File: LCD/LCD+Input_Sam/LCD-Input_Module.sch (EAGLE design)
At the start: 23 parts

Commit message: LCD PCB final touches
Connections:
- removed net N$1: JP2.3
- removed net N$2: JP2.2
- removed net N$3: JP2.1
- removed net N$8: JP2.4
- net !RES: now also JP2.3
- net SA0: now also JP2.4
- net SCL: now also JP2.2
- net SDA: now also JP2.1
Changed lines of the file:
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@@
 <grid distance="0.1" unitdist="inch" unit="inch" style="lines" multiple="1" display="no" altdistance="0.01" altunitdist="inch" altunit="inch"/>
 <layers>
-<layer number="1" name="Top" color="4" fill="1" visible="no" active="no"/>
-<layer number="16" name="Bottom" color="1" fill="1" visible="no" active="no"/>
-<layer number="17" name="Pads" color="2" fill="1" visible="no" active="no"/>
-<layer number="18" name="Vias" color="2" fill="1" visible="no" active="no"/>
-<layer number="19" name="Unrouted" color="6" fill="1" visible="no" active="no"/>
-<layer number="20" name="Dimension" color="24" fill="1" visible="no" active="no"/>
-<layer number="21" name="tPlace" color="7" fill="1" visible="no" active="no"/>
-<layer number="22" name="bPlace" color="7" fill="1" visible="no" active="no"/>
-<layer number="23" name="tOrigins" color="15" fill="1" visible="no" active="no"/>
-<layer number="24" name="bOrigins" color="15" fill="1" visible="no" active="no"/>
-<layer number="25" name="tNames" color="7" fill="1" visible="no" active="no"/>
-<layer number="26" name="bNames" color="7" fill="1" visible="no" active="no"/>
-<layer number="27" name="tValues" color="7" fill="1" visible="no" active="no"/>
-<layer number="28" name="bValues" color="7" fill="1" visible="no" active="no"/>
+<layer number="1" name="Top" color="4" fill="1" visible="yes" active="no"/>
+<layer number="16" name="Bottom" color="1" fill="1" visible="yes" active="no"/>
+<layer number="17" name="Pads" color="2" fill="1" visible="yes" active="no"/>
+<layer number="18" name="Vias" color="2" fill="1" visible="yes" active="no"/>
+<layer number="19" name="Unrouted" color="6" fill="1" visible="yes" active="no"/>
+<layer number="20" name="Dimension" color="24" fill="1" visible="yes" active="no"/>
+<layer number="21" name="tPlace" color="7" fill="1" visible="yes" active="no"/>
+<layer number="22" name="bPlace" color="7" fill="1" visible="yes" active="no"/>
+<layer number="23" name="tOrigins" color="15" fill="1" visible="yes" active="no"/>
+<layer number="24" name="bOrigins" color="15" fill="1" visible="yes" active="no"/>
+<layer number="25" name="tNames" color="7" fill="1" visible="yes" active="no"/>
+<layer number="26" name="bNames" color="7" fill="1" visible="yes" active="no"/>
+<layer number="27" name="tValues" color="7" fill="1" visible="yes" active="no"/>
+<layer number="28" name="bValues" color="7" fill="1" visible="yes" active="no"/>
 <layer number="29" name="tStop" color="7" fill="3" visible="no" active="no"/>
 <layer number="30" name="bStop" color="7" fill="6" visible="no" active="no"/>
@@
 <layer number="35" name="tGlue" color="7" fill="4" visible="no" active="no"/>
 <layer number="36" name="bGlue" color="7" fill="5" visible="no" active="no"/>
-<layer number="37" name="tTest" color="7" fill="1" visible="no" active="no"/>
-<layer number="38" name="bTest" color="7" fill="1" visible="no" active="no"/>
+<layer number="37" name="tTest" color="7" fill="1" visible="yes" active="no"/>
+<layer number="38" name="bTest" color="7" fill="1" visible="yes" active="no"/>
 <layer number="39" name="tKeepout" color="4" fill="11" visible="no" active="no"/>
 <layer number="40" name="bKeepout" color="1" fill="11" visible="no" active="no"/>
@@
 <layer number="44" name="Drills" color="7" fill="1" visible="no" active="no"/>
 <layer number="45" name="Holes" color="7" fill="1" visible="no" active="no"/>
-<layer number="46" name="Milling" color="3" fill="1" visible="no" active="no"/>
-<layer number="47" name="Measures" color="7" fill="1" visible="no" active="no"/>
-<layer number="48" name="Document" color="7" fill="1" visible="no" active="no"/>
-<layer number="49" name="Reference" color="7" fill="1" visible="no" active="no"/>
-<layer number="51" name="tDocu" color="7" fill="1" visible="no" active="no"/>
-<layer number="52" name="bDocu" color="7" fill="1" visible="no" active="no"/>
+<layer number="46" name="Milling" color="3" fill="1" visible="yes" active="no"/>
+<layer number="47" name="Measures" color="7" fill="1" visible="yes" active="no"/>
+<layer number="48" name="Document" color="7" fill="1" visible="yes" active="no"/>
+<layer number="49" name="Reference" color="7" fill="1" visible="yes" active="no"/>
+<layer number="51" name="tDocu" color="7" fill="1" visible="yes" active="no"/>
+<layer number="52" name="bDocu" color="7" fill="1" visible="yes" active="no"/>
 <layer number="88" name="SimResults" color="9" fill="1" visible="yes" active="yes"/>
 <layer number="89" name="SimProbes" color="9" fill="1" visible="yes" active="yes"/>
@@
 <net name="SDA" class="0">
 <segment>
-<wire x1="65" y1="32.36" x2="65" y2="32.395" width="0.1524" layer="91"/>
-<label x="65.2" y="32.37" size="1.778" layer="95" rot="R180"/>
-</segment>
-<segment>
 <pinref part="U$1" gate="G$1" pin="D2"/>
 <wire x1="47.2" y1="47.565" x2="47.2" y2="46" width="0.1524" layer="91"/>
@@
 <wire x1="49" y1="46" x2="49" y2="30.48" width="0.1524" layer="91"/>
 <wire x1="49" y1="30.48" x2="48.26" y2="30.48" width="0.1524" layer="91"/>
+</segment>
+<segment>
+<pinref part="JP2" gate="A" pin="1"/>
+<wire x1="88.9" y1="33.02" x2="81.28" y2="33.02" width="0.1524" layer="91"/>
+<label x="76.2" y="33.02" size="1.778" layer="95"/>
 </segment>
 </net>
@@
 <net name="!RES" class="0">
 <segment>
-<wire x1="65.375" y1="27.28" x2="65.375" y2="27.22" width="0.1524" layer="91"/>
-<label x="65.4" y="26.82" size="1.778" layer="95" rot="R180"/>
-</segment>
-<segment>
 <pinref part="U$1" gate="G$1" pin="!RESET"/>
 <wire x1="69.66" y1="57.025" x2="69.66" y2="57" width="0.1524" layer="91"/>
@@
 <label x="73" y="57" size="1.778" layer="95"/>
 </segment>
+<segment>
+<pinref part="JP2" gate="A" pin="3"/>
+<wire x1="81.28" y1="27.94" x2="88.9" y2="27.94" width="0.1524" layer="91"/>
+<label x="73.66" y="27.94" size="1.778" layer="95"/>
+</segment>
 </net>
 <net name="SCL" class="0">
-<segment>
-<wire x1="64.875" y1="29.82" x2="64.875" y2="30.02" width="0.1524" layer="91"/>
-<label x="65.4" y="29.82" size="1.778" layer="95" rot="R180"/>
-</segment>
 <segment>
 <pinref part="R8" gate="G$1" pin="2"/>
@@
 <wire x1="51.2" y1="25.4" x2="51.2" y2="47.565" width="0.1524" layer="91"/>
 <label x="51" y="25" size="1.778" layer="95" rot="R180"/>
+</segment>
+<segment>
+<pinref part="JP2" gate="A" pin="2"/>
+<wire x1="81.28" y1="30.48" x2="88.9" y2="30.48" width="0.1524" layer="91"/>
+<label x="76.2" y="30.48" size="1.778" layer="95"/>
 </segment>
 </net>
@@
 <label x="60.96" y="45.72" size="1.778" layer="95"/>
 </segment>
-</net>
-<net name="N$1" class="0">
-<segment>
-<pinref part="JP2" gate="A" pin="3"/>
-<wire x1="66.04" y1="27.94" x2="88.9" y2="27.94" width="0.1524" layer="91"/>
-</segment>
-</net>
-<net name="N$2" class="0">
-<segment>
-<pinref part="JP2" gate="A" pin="2"/>
-<wire x1="66.04" y1="30.48" x2="88.9" y2="30.48" width="0.1524" layer="91"/>
-</segment>
-</net>
-<net name="N$3" class="0">
-<segment>
-<pinref part="JP2" gate="A" pin="1"/>
-<wire x1="66.04" y1="33.02" x2="88.9" y2="33.02" width="0.1524" layer="91"/>
-</segment>
-</net>
-<net name="N$8" class="0">
 <segment>
 <pinref part="JP2" gate="A" pin="4"/>
-<wire x1="88.9" y1="25.4" x2="66.04" y2="25.4" width="0.1524" layer="91"/>
-</segment>
-</net>
+<wire x1="88.9" y1="25.4" x2="81.28" y2="25.4" width="0.1524" layer="91"/>
+<label x="76.2" y="25.4" size="1.778" layer="95"/>
+</segment>
+</net>

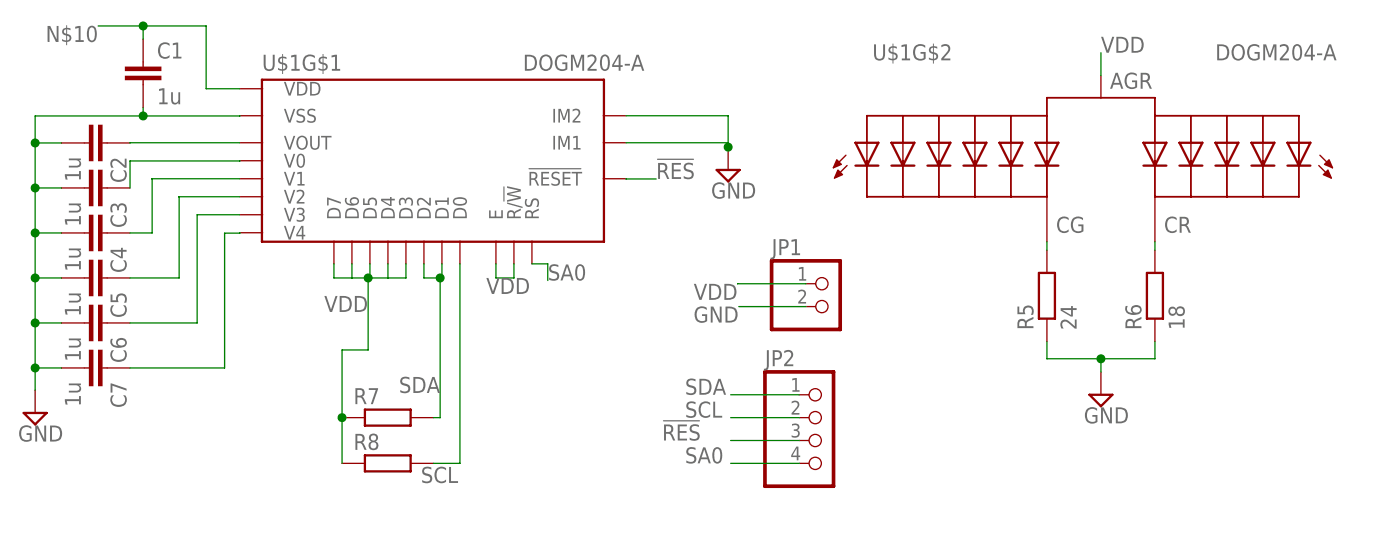
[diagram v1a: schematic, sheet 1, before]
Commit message: LCD PCB changes according to Robins suggestions. Still pending one thing
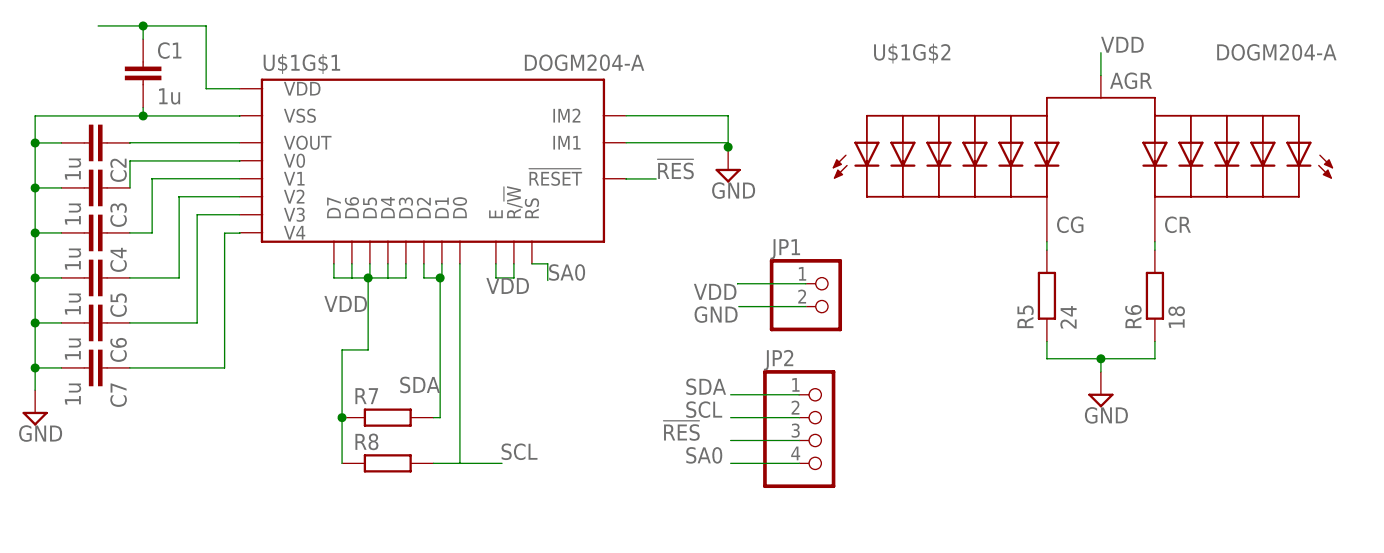
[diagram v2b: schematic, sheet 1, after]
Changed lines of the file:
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@@
 <grid distance="0.1" unitdist="inch" unit="inch" style="lines" multiple="1" display="no" altdistance="0.01" altunitdist="inch" altunit="inch"/>
 <layers>
-<layer number="1" name="Top" color="4" fill="1" visible="yes" active="no"/>
-<layer number="16" name="Bottom" color="1" fill="1" visible="yes" active="no"/>
-<layer number="17" name="Pads" color="2" fill="1" visible="yes" active="no"/>
-<layer number="18" name="Vias" color="2" fill="1" visible="yes" active="no"/>
-<layer number="19" name="Unrouted" color="6" fill="1" visible="yes" active="no"/>
-<layer number="20" name="Dimension" color="24" fill="1" visible="yes" active="no"/>
-<layer number="21" name="tPlace" color="7" fill="1" visible="yes" active="no"/>
-<layer number="22" name="bPlace" color="7" fill="1" visible="yes" active="no"/>
-<layer number="23" name="tOrigins" color="15" fill="1" visible="yes" active="no"/>
-<layer number="24" name="bOrigins" color="15" fill="1" visible="yes" active="no"/>
-<layer number="25" name="tNames" color="7" fill="1" visible="yes" active="no"/>
-<layer number="26" name="bNames" color="7" fill="1" visible="yes" active="no"/>
-<layer number="27" name="tValues" color="7" fill="1" visible="yes" active="no"/>
-<layer number="28" name="bValues" color="7" fill="1" visible="yes" active="no"/>
+<layer number="1" name="Top" color="4" fill="1" visible="no" active="no"/>
+<layer number="16" name="Bottom" color="1" fill="1" visible="no" active="no"/>
+<layer number="17" name="Pads" color="2" fill="1" visible="no" active="no"/>
+<layer number="18" name="Vias" color="2" fill="1" visible="no" active="no"/>
+<layer number="19" name="Unrouted" color="6" fill="1" visible="no" active="no"/>
+<layer number="20" name="Dimension" color="24" fill="1" visible="no" active="no"/>
+<layer number="21" name="tPlace" color="7" fill="1" visible="no" active="no"/>
+<layer number="22" name="bPlace" color="7" fill="1" visible="no" active="no"/>
+<layer number="23" name="tOrigins" color="15" fill="1" visible="no" active="no"/>
+<layer number="24" name="bOrigins" color="15" fill="1" visible="no" active="no"/>
+<layer number="25" name="tNames" color="7" fill="1" visible="no" active="no"/>
+<layer number="26" name="bNames" color="7" fill="1" visible="no" active="no"/>
+<layer number="27" name="tValues" color="7" fill="1" visible="no" active="no"/>
+<layer number="28" name="bValues" color="7" fill="1" visible="no" active="no"/>
 <layer number="29" name="tStop" color="7" fill="3" visible="no" active="no"/>
 <layer number="30" name="bStop" color="7" fill="6" visible="no" active="no"/>
@@
 <layer number="35" name="tGlue" color="7" fill="4" visible="no" active="no"/>
 <layer number="36" name="bGlue" color="7" fill="5" visible="no" active="no"/>
-<layer number="37" name="tTest" color="7" fill="1" visible="yes" active="no"/>
-<layer number="38" name="bTest" color="7" fill="1" visible="yes" active="no"/>
+<layer number="37" name="tTest" color="7" fill="1" visible="no" active="no"/>
+<layer number="38" name="bTest" color="7" fill="1" visible="no" active="no"/>
 <layer number="39" name="tKeepout" color="4" fill="11" visible="no" active="no"/>
 <layer number="40" name="bKeepout" color="1" fill="11" visible="no" active="no"/>
@@
 <layer number="44" name="Drills" color="7" fill="1" visible="no" active="no"/>
 <layer number="45" name="Holes" color="7" fill="1" visible="no" active="no"/>
-<layer number="46" name="Milling" color="3" fill="1" visible="yes" active="no"/>
-<layer number="47" name="Measures" color="7" fill="1" visible="yes" active="no"/>
-<layer number="48" name="Document" color="7" fill="1" visible="yes" active="no"/>
-<layer number="49" name="Reference" color="7" fill="1" visible="yes" active="no"/>
-<layer number="51" name="tDocu" color="7" fill="1" visible="yes" active="no"/>
-<layer number="52" name="bDocu" color="7" fill="1" visible="yes" active="no"/>
+<layer number="46" name="Milling" color="3" fill="1" visible="no" active="no"/>
+<layer number="47" name="Measures" color="7" fill="1" visible="no" active="no"/>
+<layer number="48" name="Document" color="7" fill="1" visible="no" active="no"/>
+<layer number="49" name="Reference" color="7" fill="1" visible="no" active="no"/>
+<layer number="51" name="tDocu" color="7" fill="1" visible="no" active="no"/>
+<layer number="52" name="bDocu" color="7" fill="1" visible="no" active="no"/>
 <layer number="88" name="SimResults" color="9" fill="1" visible="yes" active="yes"/>
 <layer number="89" name="SimProbes" color="9" fill="1" visible="yes" active="yes"/>
@@
 <classes>
 <class number="0" name="default" width="0" drill="0">
+<clearance class="0" value="0.2"/>
 </class>
 </classes>
@@
 <wire x1="48.26" y1="25.4" x2="51.2" y2="25.4" width="0.1524" layer="91"/>
 <wire x1="51.2" y1="25.4" x2="51.2" y2="47.565" width="0.1524" layer="91"/>
-<label x="51" y="25" size="1.778" layer="95" rot="R180"/>
+<label x="55.68" y="25.8" size="1.778" layer="95"/>
+<wire x1="51.2" y1="25.4" x2="55.88" y2="25.4" width="0.1524" layer="91"/>
 </segment>
 <segment>
@@
 <wire x1="16" y1="72.54" x2="16" y2="74" width="0.1524" layer="91"/>
 <wire x1="16" y1="74" x2="11" y2="74" width="0.1524" layer="91"/>
-<label x="11" y="74" size="1.778" layer="95" rot="R180"/>
 <pinref part="U$1" gate="G$1" pin="VDD"/>
 <wire x1="26.74" y1="67.025" x2="23" y2="67.025" width="0.1524" layer="91"/>
